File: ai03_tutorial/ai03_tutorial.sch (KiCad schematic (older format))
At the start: 24 parts, among them SW1 SW_Push, U1 ATmega32U4-AU, Y1 16Mhz

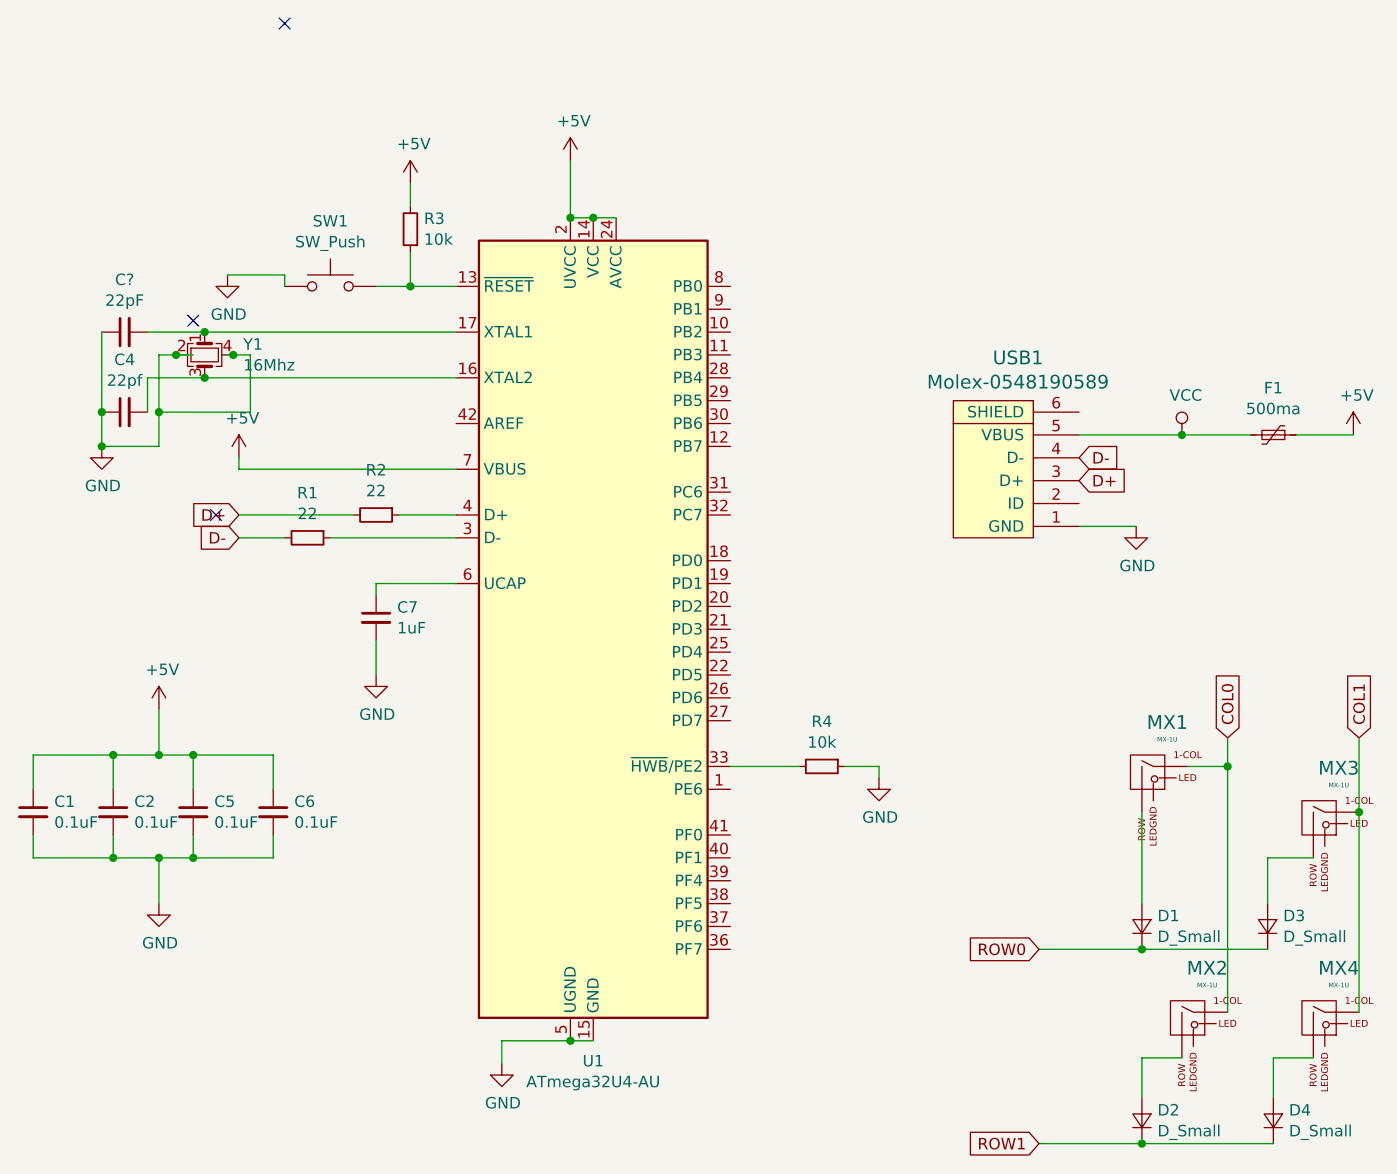
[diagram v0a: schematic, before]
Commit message: Add new usb connector and plug keycaps
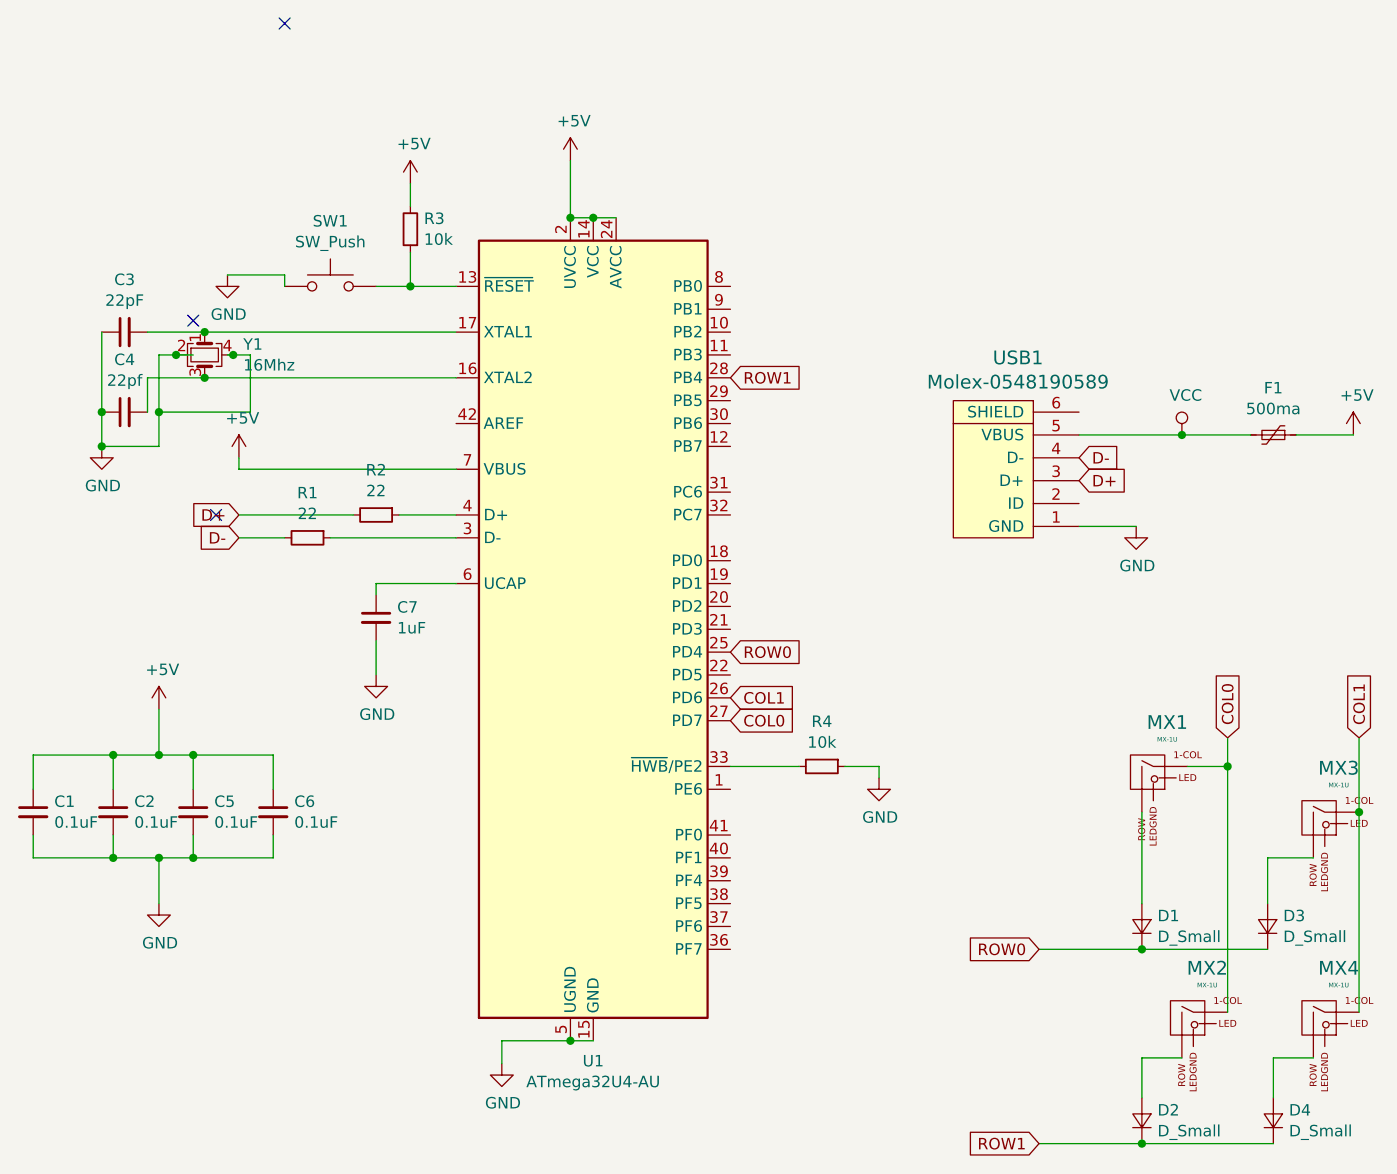
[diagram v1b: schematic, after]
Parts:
- USB1: footprint random-keyboard-parts:Molex-0548190589 -> Connector_USB:USB_Micro-B_Molex-105017-0001
- gave numbers to parts that had none: 1
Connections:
- net COL0: now also U1.27 (PD7)
- net COL1: now also U1.26 (PD6)
- net ROW0: now also U1.25 (PD4)
- net ROW1: now also U1.28 (PB4)
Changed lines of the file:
@@
 EESchema Schematic File Version 4
+LIBS:ai03_tutorial-cache
 EELAYER 29 0
 EELAYER END
@@
 F 0 "USB1" V 8662 2867 60  0000 C CNN
 F 1 "Molex-0548190589" V 8556 2867 60  0000 C CNN
-F 2 "random-keyboard-parts:Molex-0548190589" H 8125 2900 60  0001 C CNN
+F 2 "Connector_USB:USB_Micro-B_Molex-105017-0001" H 8125 2900 60  0001 C CNN
 F 3 "" H 8125 2900 60  0001 C CNN
 	1    8125 2900
@@
 $EndComp
 $Comp
-L Device:C_Small C?
+L Device:C_Small C3
 U 1 1 5C669A95
 P 4250 2250
-F 0 "C?" V 4479 2250 50  0000 C CNN
+F 0 "C3" V 4479 2250 50  0000 C CNN
 F 1 "22pF" V 4388 2250 50  0000 C CNN
 F 2 "Capacitors_SMD:C_0805" H 4250 2250 50  0001 C CNN
@@
 	0    -1   -1   0
 $EndComp
+Text GLabel 6900 3850 2    50   Input ~ 0
+COL1
+Text GLabel 6900 3950 2    50   Input ~ 0
+COL0
+Text GLabel 6900 3650 2    50   Input ~ 0
+ROW0
+Text GLabel 6900 2450 2    50   Input ~ 0
+ROW1
 $EndSCHEMATC
